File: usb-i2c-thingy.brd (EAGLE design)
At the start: 40.6 x 19.1 mm, 26 parts, among them IC1 ATTINY85, J1 10103592-0001LF, Q1 220mA/50V/3.5Ω, Q2 220mA/50V/3.5Ω, U1 CJT1117-3.3-SOT223, X1 STEREOJACK

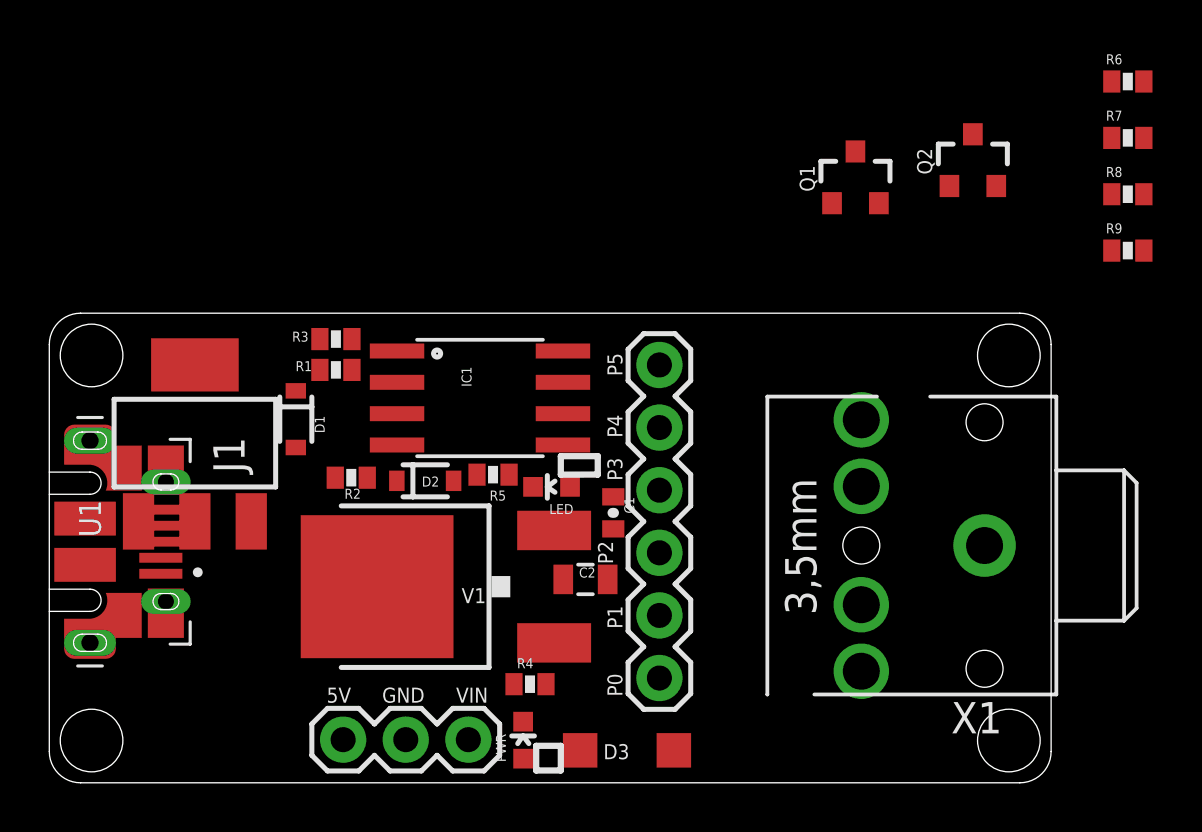
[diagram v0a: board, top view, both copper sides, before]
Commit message: Change dimensions, add 603 parts, add SDA/SCL hookup on schematic, jiggle around layout.
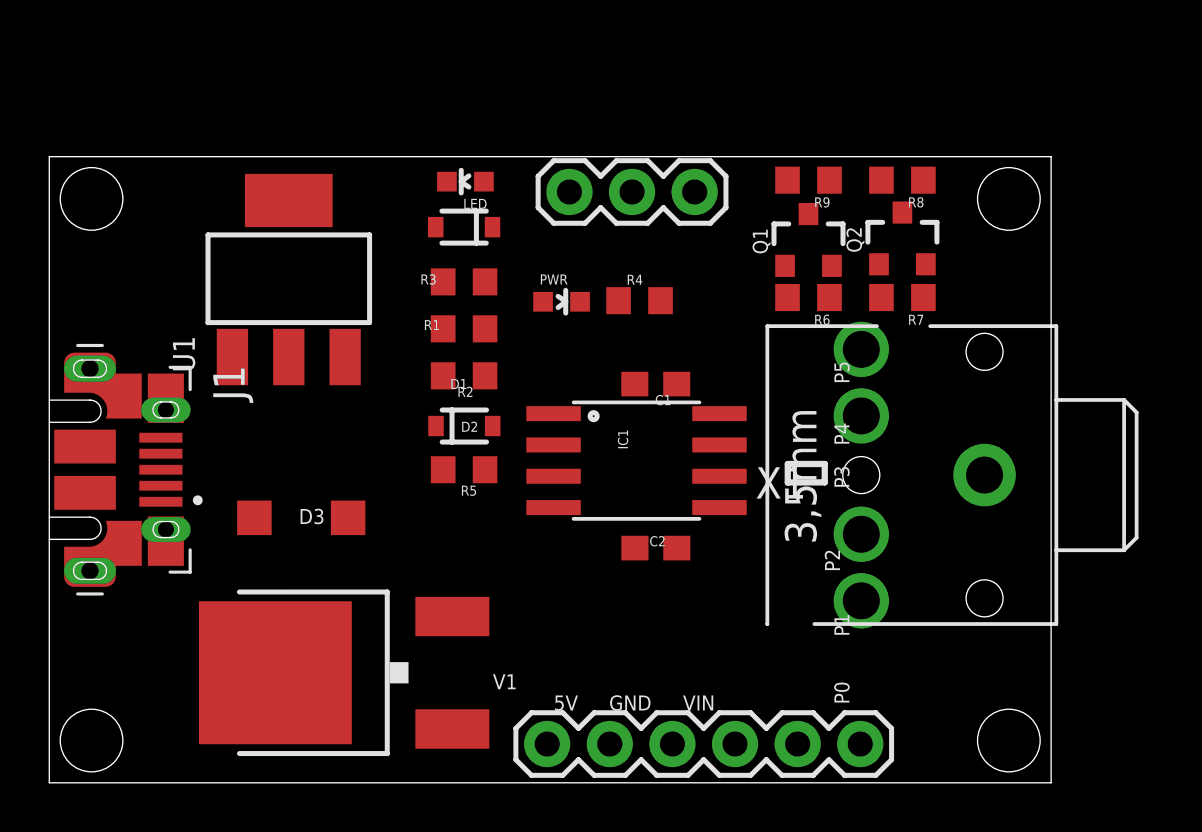
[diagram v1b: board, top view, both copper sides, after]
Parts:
- C1: device SparkFun:0402-CAP -> rcl:C0603
- C2: device SparkFun:0805 -> rcl:C0603
- R1, R2, R3, R4, R5, R6, R7, R8, R9: device SparkFun:0402-RES -> adafruit:R0603
- moved JP2 22.6 mm to (21.1, 24.0), turned to 0 degrees
- moved PWR 17.9 mm to (20.8, 19.5), turned to 270 degrees
- moved D3 16.2 mm to (10.2, 10.7), turned to 0 degrees
- moved R4 16.2 mm to (23.9, 19.6)
- moved R6 15.6 mm to (30.8, 19.7), turned to 180 degrees
- moved R9 13.3 mm to (30.8, 24.4), turned to 180 degrees
- moved LED 12.9 mm to (16.9, 24.4)
- moved R7 11.2 mm to (34.6, 19.7), turned to 180 degrees
- moved D1 10.4 mm to (16.8, 22.5), turned to 180 degrees
- moved R8 9.16 mm to (34.6, 24.4), turned to 180 degrees
- moved JP3 8.58 mm to (32.9, 1.57), turned to 180 degrees
- moved U1 7.68 mm to (9.72, 20.4)
- moved IC1 6.84 mm to (23.8, 13.1)
- moved R2 6.17 mm to (16.8, 16.5)
- moved R3 5.69 mm to (16.8, 20.3)
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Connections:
- removed net N$3: IC1.5, JP3.1
- removed net N$5: IC1.7, JP3.3
- net SCL: now also IC1.7, JP3.3
- net SDA: now also IC1.5, JP3.1
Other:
- board size 40.6 x 19.1 mm -> 40.6 x 25.4 mm
- board text removed: "digistu.mp/digispark"

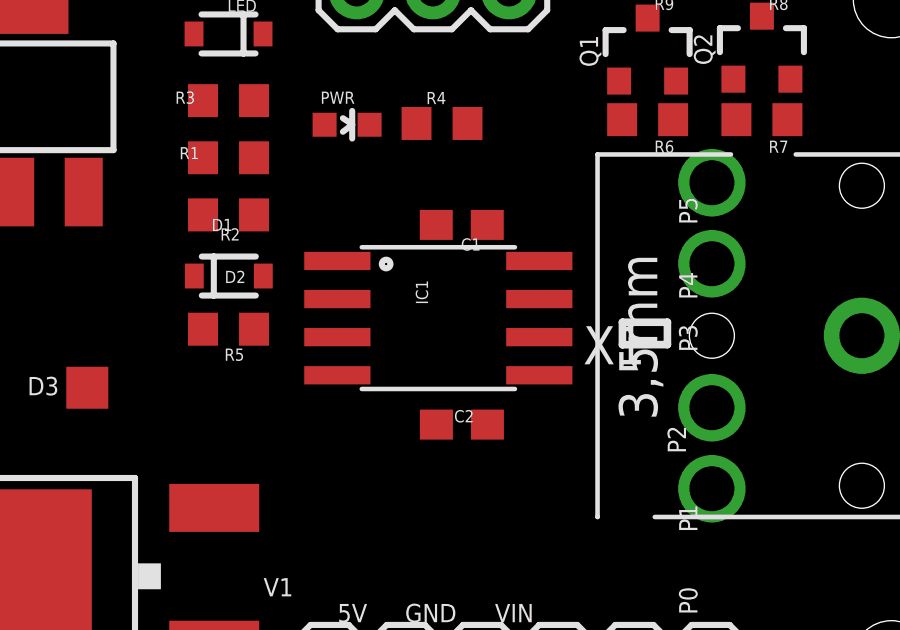
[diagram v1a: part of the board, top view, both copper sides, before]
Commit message: Remove DS stuff from board, be sure to credit as part of CCBYSA licensing in future.
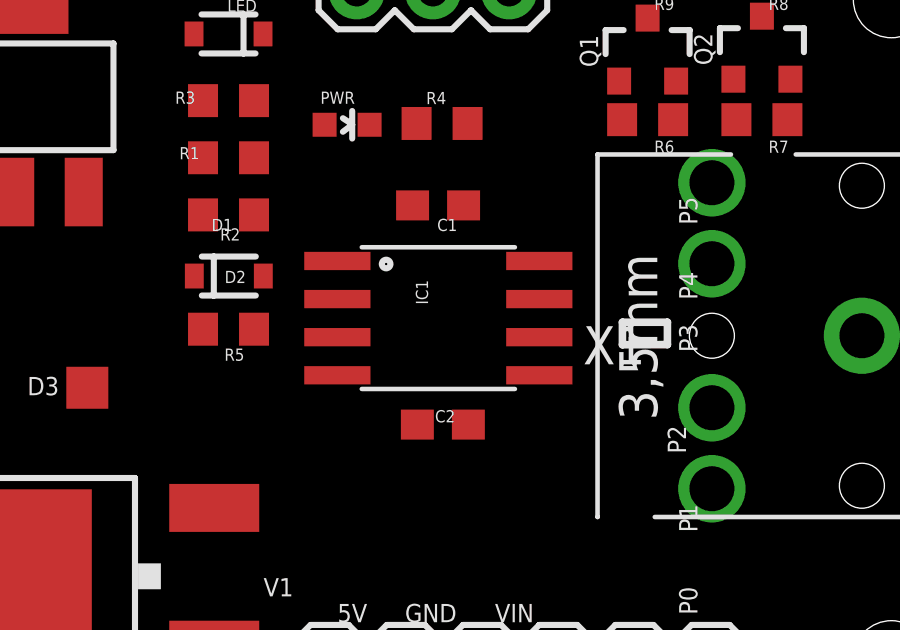
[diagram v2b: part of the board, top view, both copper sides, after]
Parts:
- moved C1 1.02 mm to (23.8, 16.8)
- moved C2 0.64 mm to (24.0, 9.52)
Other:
- board text removed: "Created by"
- board text removed: "Created by Erik Kettenbugr, Digistump LLC - digistump.com 2012"
- board text removed: "Digispark name. logo and Digistump name, logo Copyright 2013 Digistump LLC All Rights Reserved"
- board text removed: "Digistump LLC"
- board text removed: "Erik Kettenburg"
- board text removed: "For full details and license information please see http://digistump.com/wiki/digispark/policy"
- board text removed: "Getting started:"
- board text removed: "RoHS"
- board text removed: "The Digispark and Digistump names and logos (or derivatives thereof) may not be used as part of the name of a product, company, or domain name without express written permission."
- board text removed: "The Digispark design (schematic, layout, concept) is licensed under the Creative Commons Attribution-ShareAlike 3.0 Unported License: http://creativecommons.org/licenses/by-sa/3.0/"
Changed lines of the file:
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@@
 <wire x1="29.9575" y1="12.1825" x2="31.4575" y2="12.1865" width="0.254" layer="21"/>
 <wire x1="31.4575" y1="12.1865" x2="31.4575" y2="12.9325" width="0.254" layer="21"/>
-<text x="23.4315" y="8.1915" size="1.27" layer="22" font="vector" ratio="15" rot="MR180">RoHS</text>
 <text x="30.9245" y="7.3025" size="0.6096" layer="22" font="vector" ratio="12" rot="MR270">PWM</text>
 <text x="31.6865" y="15.0495" size="0.6096" layer="22" font="vector" ratio="12" rot="MR270">PWM</text>
@@
 <text x="31.6865" y="4.7625" size="0.6096" layer="22" font="vector" ratio="12" rot="MR270">AREF</text>
 <text x="29.4005" y="4.5085" size="0.6096" layer="22" font="vector" ratio="12" rot="MR270">PWM</text>
-<text x="28.3845" y="17.2085" size="0.508" layer="22" rot="MR0">Created by</text>
-<text x="29.0195" y="16.4465" size="0.508" layer="22" rot="MR0">Erik Kettenburg</text>
-<text x="28.8925" y="15.6845" size="0.508" layer="22" rot="MR0">Digistump LLC</text>
-<text x="22.5425" y="13.081" size="1.016" layer="22" font="vector" ratio="15" rot="MR270">Getting started:</text>
-<text x="-13.589" y="-1.905" size="0.6096" layer="49">The Digispark design (schematic, layout, concept) is licensed under the Creative Commons Attribution-ShareAlike 3.0 Unported License: http://creativecommons.org/licenses/by-sa/3.0/</text>
-<text x="-13.589" y="-3.302" size="0.6096" layer="49">The Digispark and Digistump names and logos (or derivatives thereof) may not be used as part of the name of a product, company, or domain name without express written permission.</text>
-<text x="-13.589" y="-4.572" size="0.6096" layer="49">Digispark name. logo and Digistump name, logo Copyright 2013 Digistump LLC All Rights Reserved</text>
-<text x="-13.589" y="-5.842" size="0.6096" layer="49">For full details and license information please see http://digistump.com/wiki/digispark/policy</text>
-<text x="-13.589" y="-6.985" size="0.6096" layer="49">Created by Erik Kettenbugr, Digistump LLC - digistump.com 2012</text>
 <hole x="1.7145" y="23.6855" drill="2.54"/>
 <hole x="1.7145" y="1.7145" drill="2.54"/>
@@
 <attribute name="VALUE" x="17.8435" y="23.9395" size="0.4064" layer="27" rot="R180"/>
 </element>
-<element name="C1" library="rcl" library_urn="urn:adsk.eagle:library:334" package="C0603" package3d_urn="urn:adsk.eagle:package:23616/2" value="0.1uf" x="24.6031" y="16.1755" smashed="yes" rot="R180">
-<attribute name="NAME" x="25.2421" y="15.727" size="0.4064" layer="25" rot="R180"/>
-<attribute name="POPULARITY" value="73" x="24.6031" y="16.1755" size="1.778" layer="27" rot="R180" display="off"/>
-<attribute name="SPICEPREFIX" value="C" x="24.6031" y="16.1755" size="1.778" layer="27" rot="R180" display="off"/>
-<attribute name="VALUE" x="25.6826" y="17.3185" size="0.4064" layer="27" rot="R180"/>
+<element name="C1" library="rcl" library_urn="urn:adsk.eagle:library:334" package="C0603" package3d_urn="urn:adsk.eagle:package:23616/2" value="0.1uf" x="23.8125" y="16.8275" smashed="yes" rot="R180">
+<attribute name="NAME" x="24.4515" y="16.379" size="0.4064" layer="25" rot="R180"/>
+<attribute name="POPULARITY" value="73" x="23.8125" y="16.8275" size="1.778" layer="27" rot="R180" display="off"/>
+<attribute name="SPICEPREFIX" value="C" x="23.8125" y="16.8275" size="1.778" layer="27" rot="R180" display="off"/>
+<attribute name="VALUE" x="24.892" y="17.9705" size="0.4064" layer="27" rot="R180"/>
 </element>
 <element name="R1" library="adafruit" library_urn="urn:adsk.eagle:library:420" package="R0603" package3d_urn="urn:adsk.eagle:package:6240565/1" value="66.5R" x="16.8275" y="18.415" smashed="yes">
@@
 <attribute name="VALUE" x="25.0245" y="20.7005" size="0.4064" layer="27" rot="R180"/>
 </element>
-<element name="C2" library="rcl" library_urn="urn:adsk.eagle:library:334" package="C0603" package3d_urn="urn:adsk.eagle:package:23616/2" value="4.7uf" x="24.6075" y="9.52" smashed="yes">
-<attribute name="NAME" x="24.3455" y="9.5955" size="0.4064" layer="25"/>
-<attribute name="POPULARITY" value="73" x="24.6075" y="9.52" size="1.778" layer="27" display="off"/>
-<attribute name="SPICEPREFIX" value="C" x="24.6075" y="9.52" size="1.778" layer="27" display="off"/>
-<attribute name="VALUE" x="23.5915" y="8.123" size="0.4064" layer="27"/>
+<element name="C2" library="rcl" library_urn="urn:adsk.eagle:library:334" package="C0603" package3d_urn="urn:adsk.eagle:package:23616/2" value="4.7uf" x="23.9725" y="9.52" smashed="yes">
+<attribute name="NAME" x="23.7105" y="9.5955" size="0.4064" layer="25"/>
+<attribute name="POPULARITY" value="73" x="23.9725" y="9.52" size="1.778" layer="27" display="off"/>
+<attribute name="SPICEPREFIX" value="C" x="23.9725" y="9.52" size="1.778" layer="27" display="off"/>
+<attribute name="VALUE" x="22.9565" y="8.123" size="0.4064" layer="27"/>
 </element>
 <element name="JP2" library="SparkFun" package="1X03" value="" x="21.1" y="23.9675" smashed="yes">
@@
 <contactref element="X1" pad="1"/>
 <contactref element="U1" pad="1"/>
-<wire x1="23.7531" y1="16.1755" x2="37.94" y2="12.4825" width="0" layer="19" extent="1-1"/>
-<wire x1="25.4575" y1="9.52" x2="23.7531" y2="16.1755" width="0" layer="19" extent="1-1"/>
-<wire x1="24.795" y1="19.5575" x2="25.4575" y2="9.52" width="0" layer="19" extent="1-1"/>
-<wire x1="15.9775" y1="12.7" x2="23.7531" y2="16.1755" width="0" layer="19" extent="1-1"/>
+<wire x1="22.9625" y1="16.8275" x2="37.94" y2="12.4825" width="0" layer="19" extent="1-1"/>
+<wire x1="24.8225" y1="9.52" x2="22.9625" y2="16.8275" width="0" layer="19" extent="1-1"/>
+<wire x1="24.795" y1="19.5575" x2="24.8225" y2="9.52" width="0" layer="19" extent="1-1"/>
+<wire x1="15.9775" y1="12.7" x2="22.9625" y2="16.8275" width="0" layer="19" extent="1-1"/>
 <wire x1="17.9875" y1="14.4725" x2="15.9775" y2="12.7" width="0" layer="19" extent="1-1"/>
 <wire x1="20.4558" y1="11.1646" x2="17.9875" y2="14.4725" width="0" layer="19" extent="1-1"/>
@@
 <contactref element="R9" pad="2"/>
 <wire x1="29.9475" y1="24.4475" x2="33.7575" y2="24.4475" width="0" layer="19" extent="1-1"/>
-<wire x1="25.4531" y1="16.1755" x2="29.9475" y2="24.4475" width="0" layer="19" extent="1-1"/>
-<wire x1="16.3509" y1="6.7435" x2="25.4531" y2="16.1755" width="0" layer="19" extent="1-1"/>
-<wire x1="23.7575" y1="9.52" x2="16.3509" y2="6.7435" width="0" layer="19" extent="1-1"/>
-<wire x1="27.1868" y1="14.9746" x2="25.4531" y2="16.1755" width="0" layer="19" extent="1-1"/>
-<wire x1="12.1206" y1="10.7486" x2="23.7575" y2="9.52" width="0" layer="19" extent="1-1"/>
+<wire x1="24.6625" y1="16.8275" x2="29.9475" y2="24.4475" width="0" layer="19" extent="1-1"/>
+<wire x1="16.3509" y1="6.7435" x2="24.6625" y2="16.8275" width="0" layer="19" extent="1-1"/>
+<wire x1="23.1225" y1="9.52" x2="16.3509" y2="6.7435" width="0" layer="19" extent="1-1"/>
+<wire x1="27.1868" y1="14.9746" x2="24.6625" y2="16.8275" width="0" layer="19" extent="1-1"/>
+<wire x1="12.1206" y1="10.7486" x2="23.1225" y2="9.52" width="0" layer="19" extent="1-1"/>
 <wire x1="20.03" y1="19.515" x2="12.1206" y2="10.7486" width="0" layer="19" extent="1-1"/>
 <wire x1="26.18" y1="23.9675" x2="20.03" y2="19.515" width="0" layer="19" extent="1-1"/>

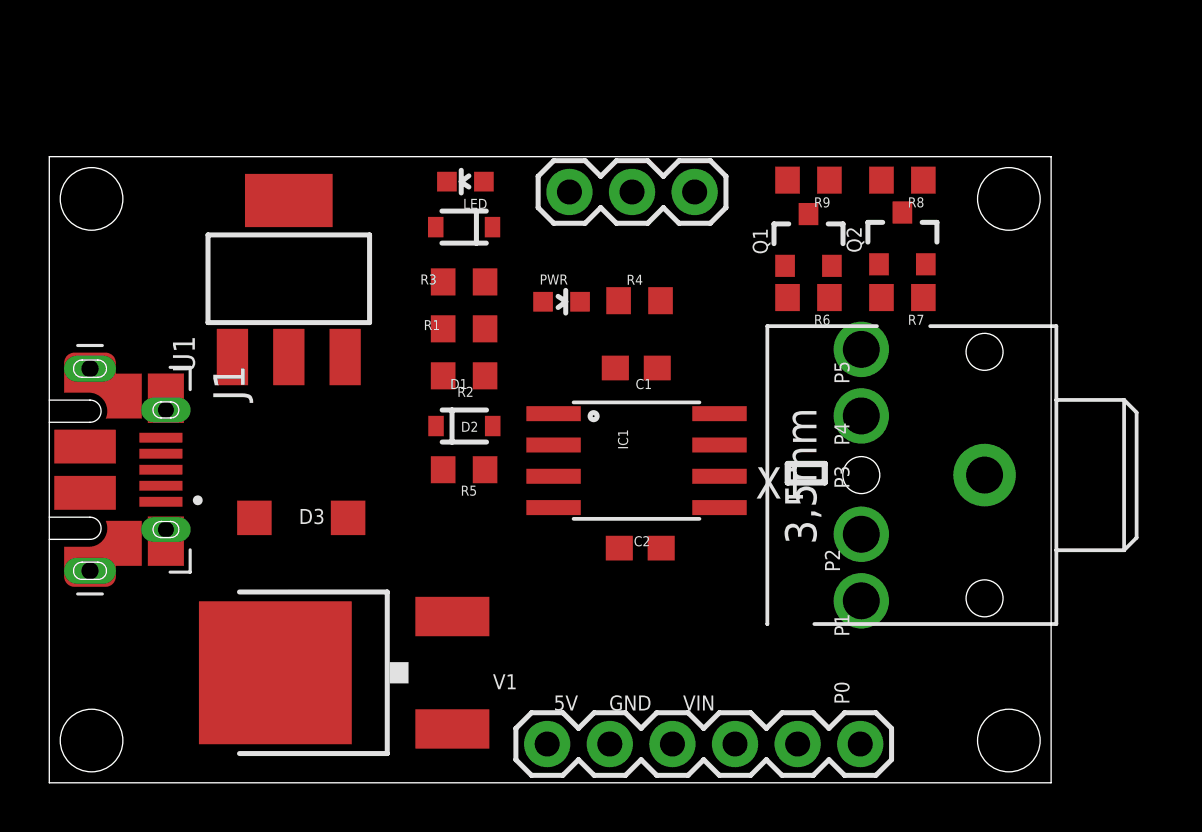
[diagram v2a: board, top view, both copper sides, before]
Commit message: M3 holes, rounded corners.
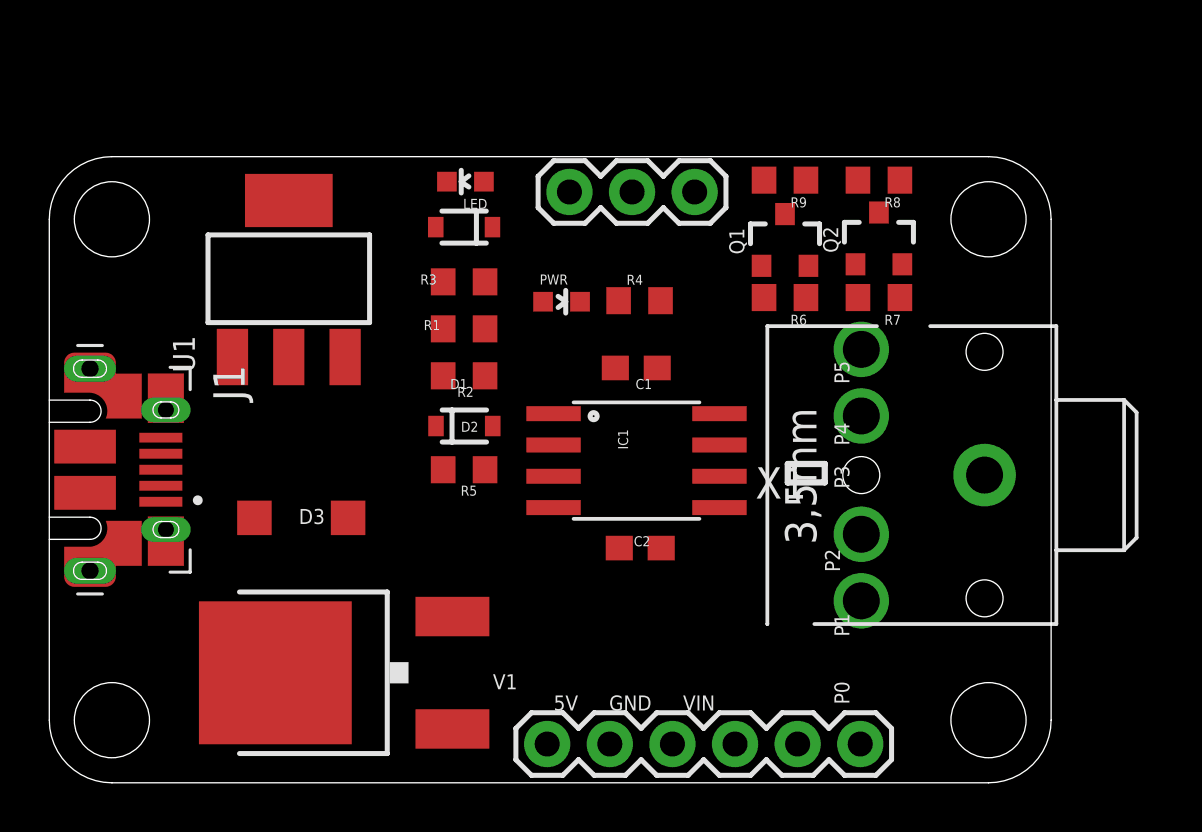
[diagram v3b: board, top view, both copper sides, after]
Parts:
- moved Q1 0.95 mm to (29.8, 22.0)
- moved Q2 0.95 mm to (33.7, 22.0)
- moved R6 0.95 mm to (29.8, 19.7)
- moved R7 0.95 mm to (33.7, 19.7)
- moved R8 0.95 mm to (33.7, 24.4)
- moved R9 0.95 mm to (29.8, 24.4)
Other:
- outline, holes or cut-outs redrawn
